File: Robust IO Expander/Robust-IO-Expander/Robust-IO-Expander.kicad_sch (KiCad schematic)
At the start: 54 parts, among them J1 Input Headers, J2 Chip Select Input, J3 Power Input, J4 SPI Input, J5 Screw_Terminal_01x16, J6 Output Screw Terminal, J7 Ouput Headers, J8 Power Input, U1 MCP23S17_SS, U10 LTV-847S, U2 MCP23S17_SS, U3 LTV-847S, U4 LTV-847S, U5 LTV-847S, U6 LTV-847S, U7 LTV-847S, U8 LTV-847S, U9 LTV-847S

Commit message: update
AD 09/10/23

finished schematic and all components on board
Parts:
- removed J3: Power Input, Connector_PinSocket_2.54mm:PinSocket_1x02_P2.54mm_Vertical, symbol Connector:Conn_01x02_Pin
- removed J8: Power Input, symbol Connector:Screw_Terminal_01x02
- added C1: 10uF, Capacitor_SMD:C_1206_3216Metric_Pad1.33x1.80mm_HandSolder, symbol Device:C_Polarized_Small
- added C2: 22uF, Capacitor_SMD:C_1206_3216Metric_Pad1.33x1.80mm_HandSolder, symbol Device:C_Polarized_Small
- added J10: Right SPI In, Connector_PinSocket_2.54mm:PinSocket_1x04_P2.54mm_Horizontal, symbol Connector:Conn_01x04_Socket
- added J11: SPI Inputs, TerminalBlock_Phoenix:TerminalBlock_Phoenix_MKDS-1,5-3_1x03_P5.00mm_Horizontal, symbol Connector:Screw_Terminal_01x03
- added J12: Power Input, Connector_PinSocket_2.54mm:PinSocket_1x03_P2.54mm_Vertical, symbol Connector:Conn_01x03_Pin
- added J3: CS Inputs, TerminalBlock_Phoenix:TerminalBlock_Phoenix_MKDS-1,5-2_1x02_P5.00mm_Horizontal, symbol Connector:Screw_Terminal_01x02
- added J8: Power Input, TerminalBlock_Phoenix:TerminalBlock_Phoenix_MKDS-1,5-3-5.08_1x03_P5.08mm_Horizontal, symbol Connector:Screw_Terminal_01x03
- added J9: Left SPI Out, Connector_PinHeader_2.54mm:PinHeader_1x04_P2.54mm_Horizontal, symbol Connector:Conn_01x04_Pin
- added U11: AMS1117-3.3, Package_TO_SOT_SMD:SOT-223-3_TabPin2, symbol Regulator_Linear:AMS1117-3.3
- J2: value Chip Select Input -> CS Inputs
- J4: value SPI Input -> SPI Inputs; footprint (none) -> Connector_PinSocket_2.54mm:PinSocket_1x03_P2.54mm_Vertical
- J5: value Screw_Terminal_01x16 -> Input Screw Terminal; footprint (none) -> TerminalBlock_Phoenix:TerminalBlock_Phoenix_MKDS-1,5-16_1x16_P5.00mm_Horizontal
- J6: footprint (none) -> TerminalBlock_Phoenix:TerminalBlock_Phoenix_MKDS-1,5-16_1x16_P5.00mm_Horizontal
- J7: footprint (none) -> Connector_PinSocket_2.54mm:PinSocket_1x16_P2.54mm_Vertical
- R1, R10, R11, R12, R13, R14, R15, R16, R17, R18, R19, R2, R20, R21, R22, R23, R24, R25, R26, R27, R28, R29, R3, R30, R31, R32, R4, R5, R6, R7, R8, R9: footprint (none) -> Resistor_SMD:R_0603_1608Metric_Pad0.98x0.95mm_HandSolder
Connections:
- net GND: now also C1.2, C2.2, J10.4 (Pin_4), J12.3 (Pin_3), J8.3 (Pin_3), J9.4 (Pin_4), U11.1 (GND)
- net InCS: now also J3.1 (Pin_1)
- net MISO: now also J10.3 (Pin_3), J11.3 (Pin_3), J9.3 (Pin_3)
- net MOSI: now also J10.2 (Pin_2), J11.2 (Pin_2), J9.2 (Pin_2)
- net OutCS: now also J3.2 (Pin_2)
- net SCK: now also J10.1 (Pin_1), J11.1 (Pin_1), J9.1 (Pin_1)
- net VCC: now also C1.1, J12.1 (Pin_1), J8.1 (Pin_1), U11.3 (VI); no longer U1.9 (VDD), U10.10, U10.12, U10.14, U10.16, U2.9 (VDD), U3.10, U3.12, U3.14, U3.16, U4.10, U4.12, U4.14, U4.16, U5.10, U5.12, U5.14, U5.16, U6.10, U6.12, U6.14, U6.16, U7.10, U7.12, U7.14, U7.16, U8.10, U8.12, U8.14, U8.16, U9.10, U9.12, U9.14, U9.16
- new net +24V: J12.2 (Pin_2), J8.2 (Pin_2), U10.10, U10.12, U10.14, U10.16, U7.10, U7.12, U7.14, U7.16, U8.10, U8.12, U8.14, U8.16, U9.10, U9.12, U9.14, U9.16
- new net +3.3V: C2.1, U1.9 (VDD), U11.2 (VO), U2.9 (VDD), U3.10, U3.12, U3.14, U3.16, U4.10, U4.12, U4.14, U4.16, U5.10, U5.12, U5.14, U5.16, U6.10, U6.12, U6.14, U6.16
- no-connect marks 0 -> 12
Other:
- note added: "10uF Tantalum Capacitor T491A106K020AT"
- note added: "22uF Tantalum Capacitor TAJA226M016RNJ"
- note added: "AMS1117 3.3V Voltage Regulator"
- note added: "I/O CONNECTORS"
- note added: "Power"
- note added: "SPI Connectors"
- note removed: "CONNECTORS"
- moved on the sheet: H1, H2, H3, J1, J2, J4, J5, J6, J7, R1, R10, R11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

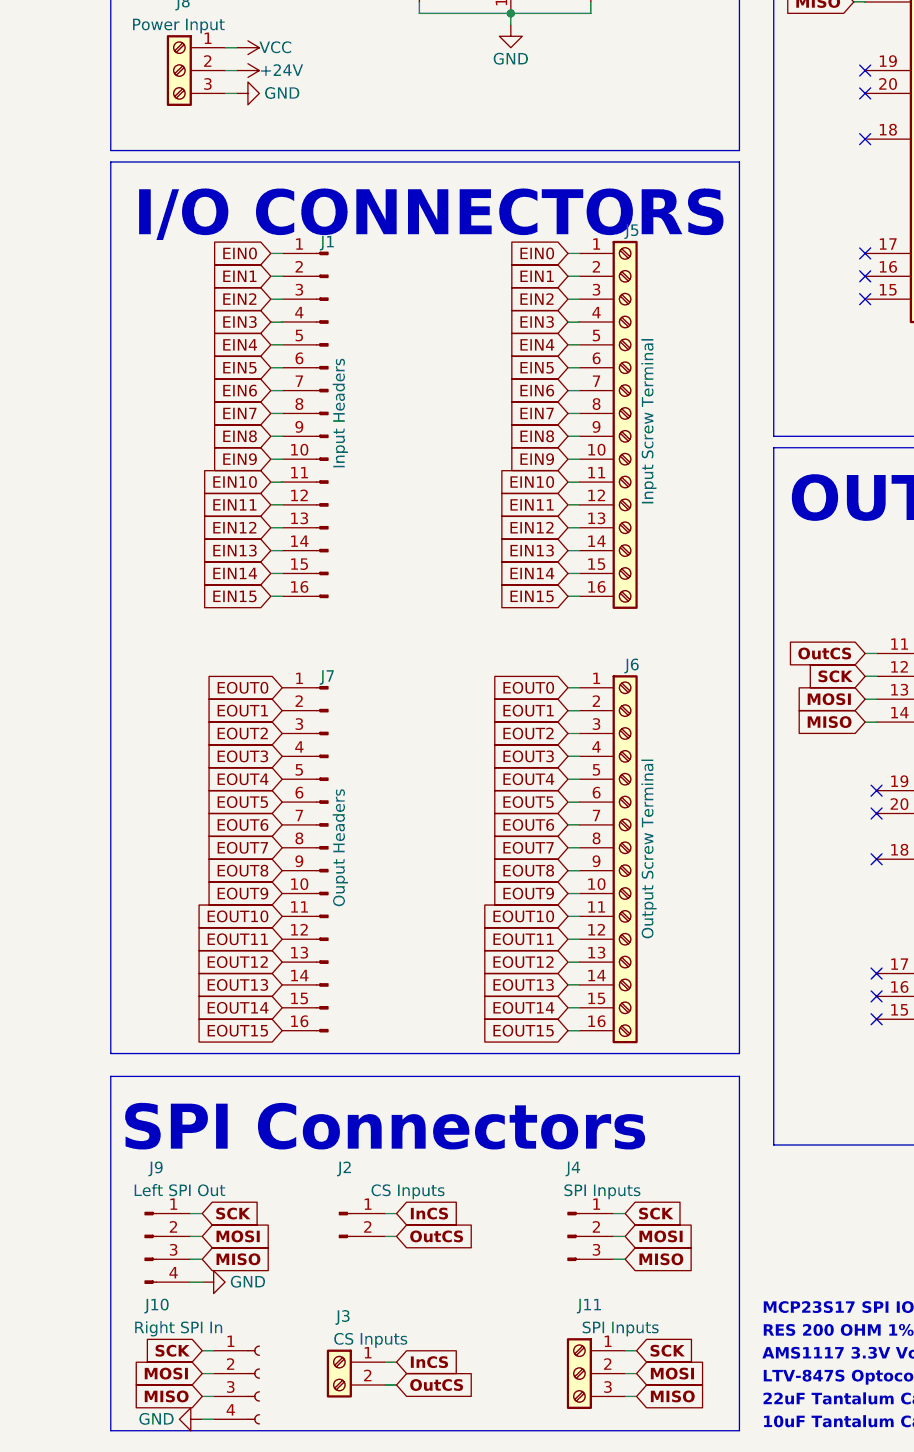
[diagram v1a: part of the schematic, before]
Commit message: Layout change
AD 15/10/23: Add Screw terminals everywhere
ESD Protection on IO and SPI Inputs
3.3v Regulator for IO power
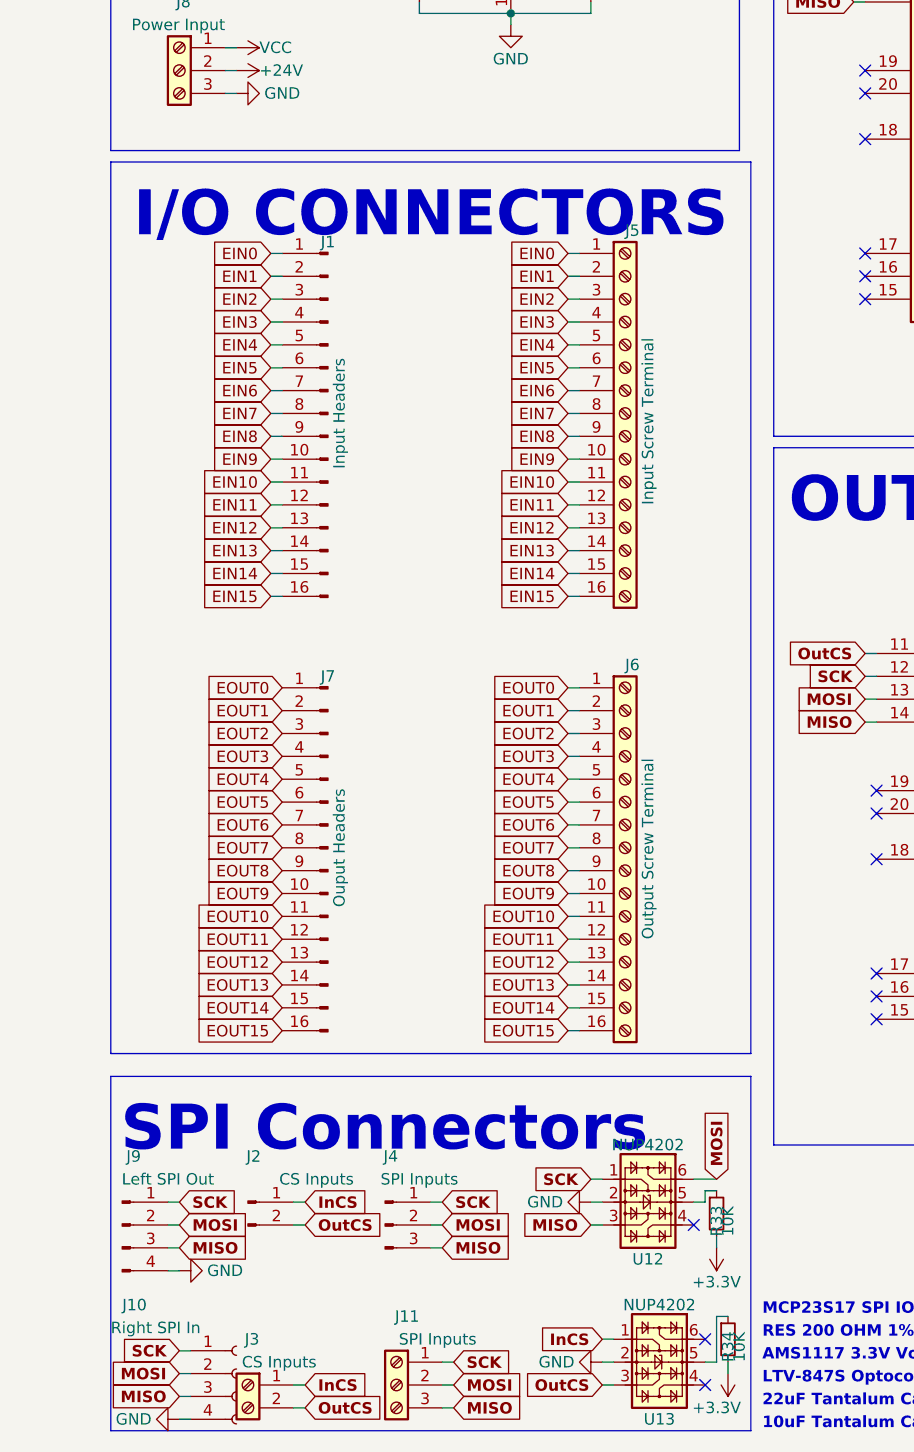
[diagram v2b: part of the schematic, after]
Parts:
- added R33, R34: 10K, Resistor_SMD:R_0603_1608Metric_Pad0.98x0.95mm_HandSolder, symbol Device:R_Small
- added U12, U13: NUP4202, Package_TO_SOT_SMD:SOT-363_SC-70-6, symbol Power_Protection:NUP4202
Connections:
- net +3.3V: now also R33.2, R34.2
- net GND: now also U12.2, U13.2
- net InCS: now also U13.1
- net MISO: now also U12.3
- net MOSI: now also U12.6
- net OutCS: now also U13.3
- net SCK: now also U12.1
- new net: R34.1, U13.5
- new net: R33.1, U12.5
- no-connect marks 12 -> 15
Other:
- moved on the sheet: J10, J11, J2, J3, J4, J9

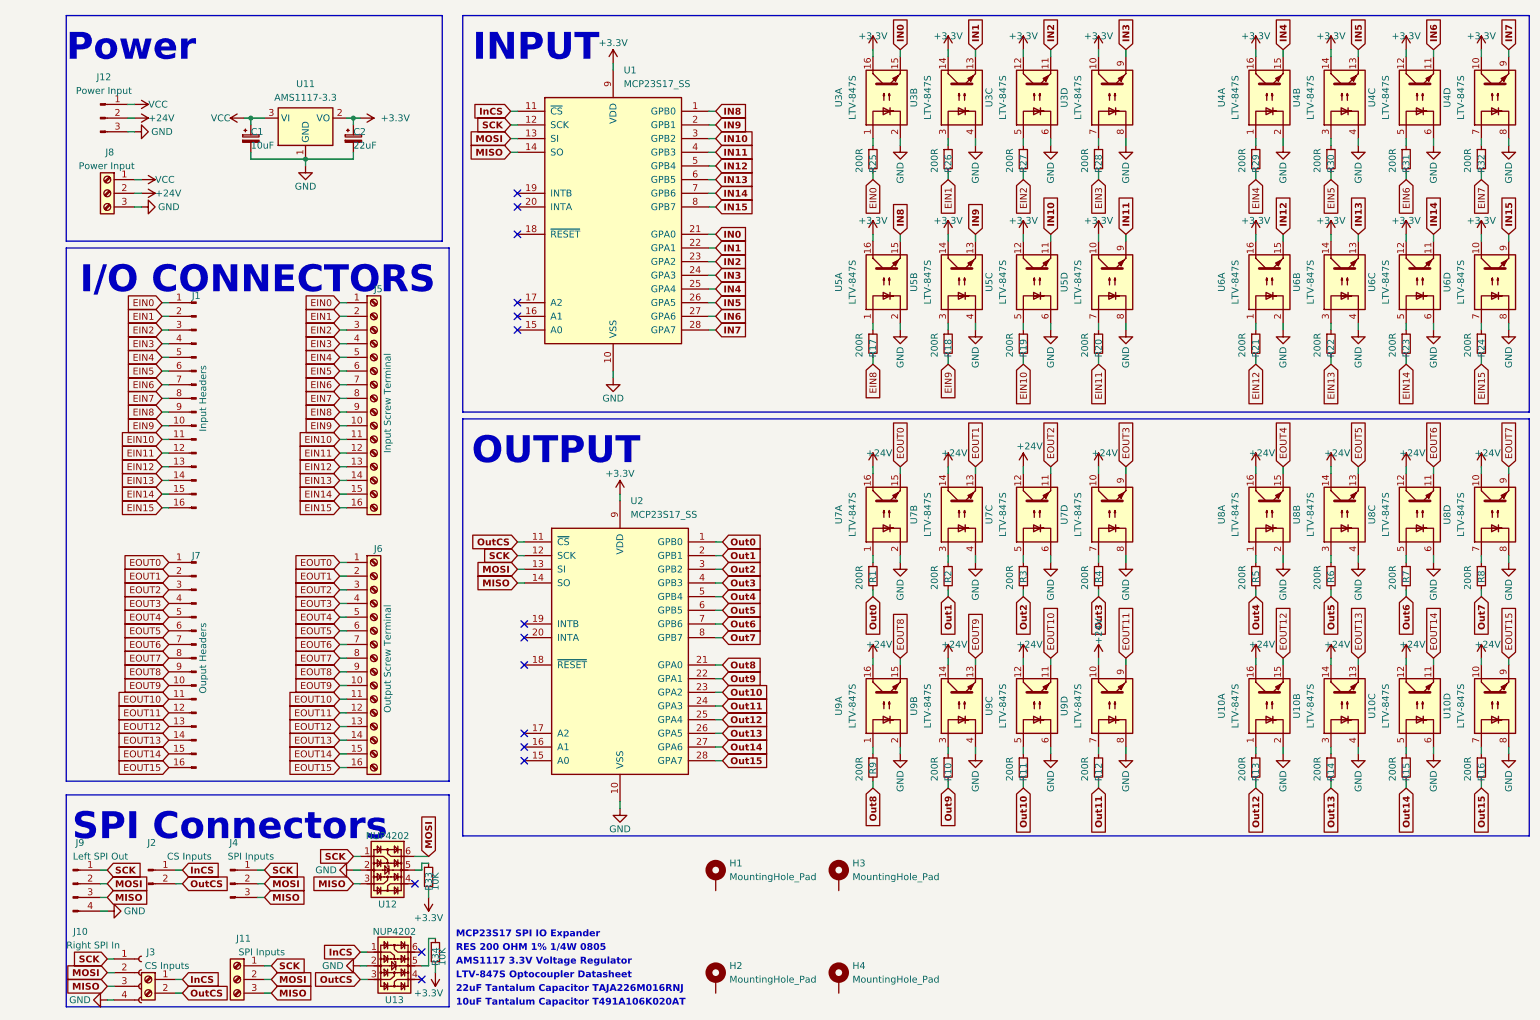
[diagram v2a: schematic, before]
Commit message: Design Complete
AD 10/12/23:
Design Finalised
BOM Created
Gerber and POS Files Generate
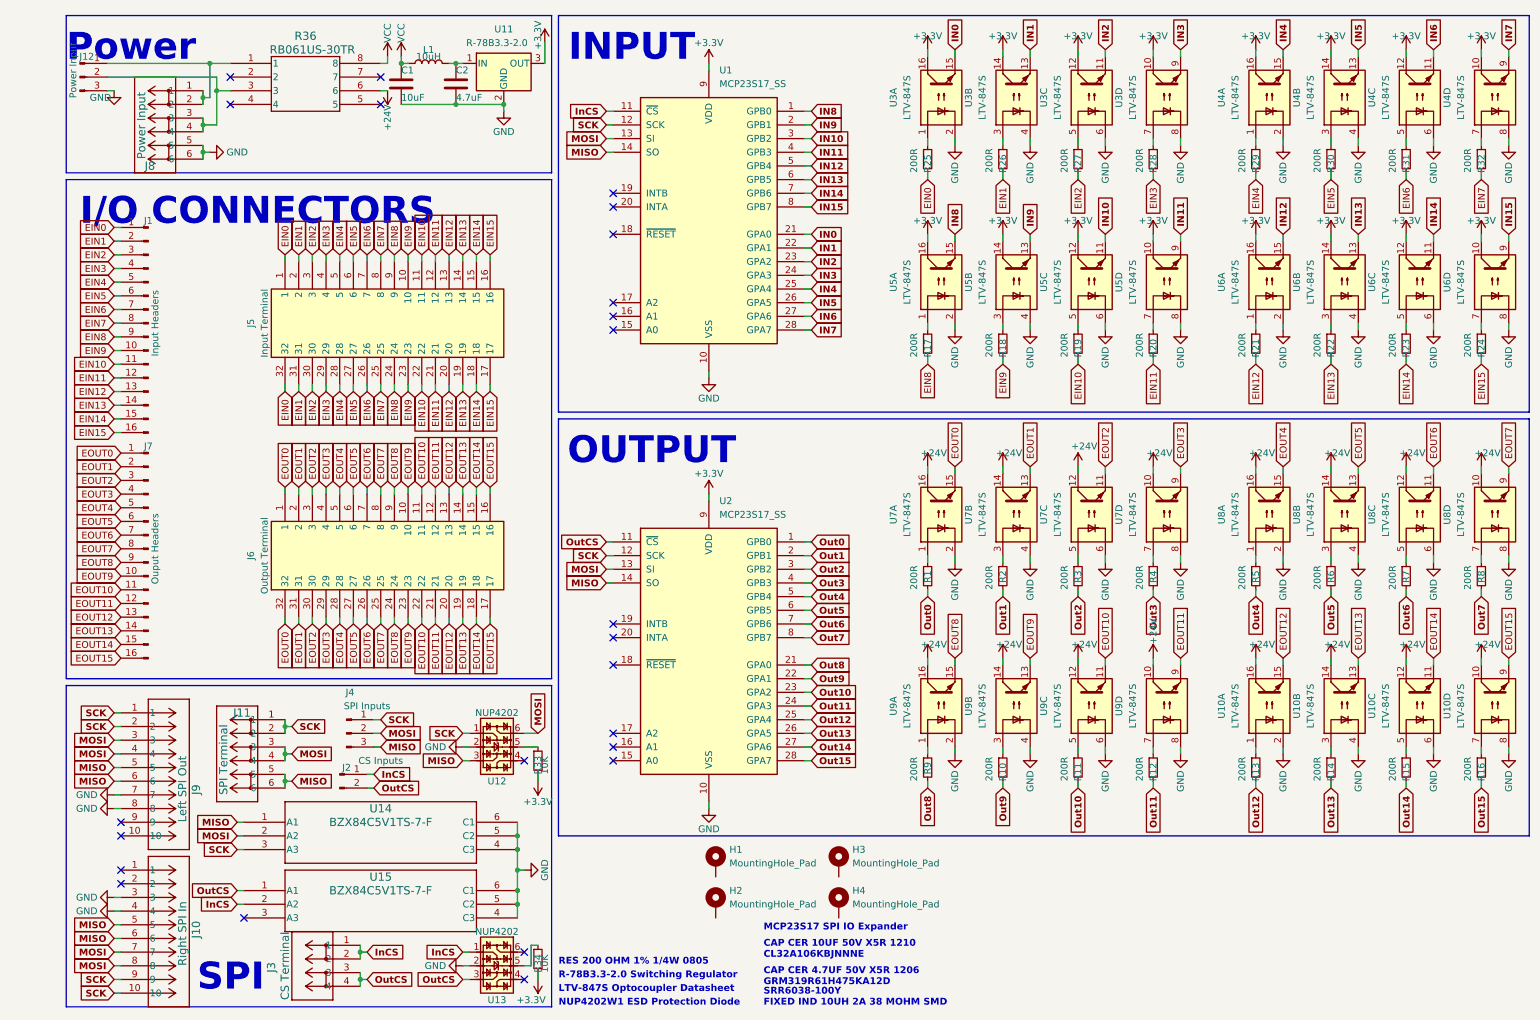
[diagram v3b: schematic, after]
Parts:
- removed C1: 10uF, Capacitor_SMD:C_1206_3216Metric_Pad1.33x1.80mm_HandSolder, symbol Device:C_Polarized_Small
- removed C2: 22uF, Capacitor_SMD:C_1206_3216Metric_Pad1.33x1.80mm_HandSolder, symbol Device:C_Polarized_Small
- removed J10: Right SPI In, Connector_PinSocket_2.54mm:PinSocket_1x04_P2.54mm_Horizontal, symbol Connector:Conn_01x04_Socket
- removed J11: SPI Inputs, TerminalBlock_Phoenix:TerminalBlock_Phoenix_MKDS-1,5-3_1x03_P5.00mm_Horizontal, symbol Connector:Screw_Terminal_01x03
- removed J3: CS Inputs, TerminalBlock_Phoenix:TerminalBlock_Phoenix_MKDS-1,5-2_1x02_P5.00mm_Horizontal, symbol Connector:Screw_Terminal_01x02
- removed J5: Input Screw Terminal, TerminalBlock_Phoenix:TerminalBlock_Phoenix_MKDS-1,5-16_1x16_P5.00mm_Horizontal, symbol Connector:Screw_Terminal_01x16
- removed J6: Output Screw Terminal, TerminalBlock_Phoenix:TerminalBlock_Phoenix_MKDS-1,5-16_1x16_P5.00mm_Horizontal, symbol Connector:Screw_Terminal_01x16
- removed J8: Power Input, TerminalBlock_Phoenix:TerminalBlock_Phoenix_MKDS-1,5-3-5.08_1x03_P5.08mm_Horizontal, symbol Connector:Screw_Terminal_01x03
- removed J9: Left SPI Out, Connector_PinHeader_2.54mm:PinHeader_1x04_P2.54mm_Horizontal, symbol Connector:Conn_01x04_Pin
- removed U11: AMS1117-3.3, Package_TO_SOT_SMD:SOT-223-3_TabPin2, symbol Regulator_Linear:AMS1117-3.3
- added C1: 10uF, Capacitor_SMD:C_1210_3225Metric_Pad1.33x2.70mm_HandSolder, symbol Device:C
- added C2: 4.7uF, Capacitor_SMD:C_1206_3216Metric_Pad1.33x1.80mm_HandSolder, symbol Device:C
- added J10: Right SPI In, LS2_105_01_F_D_RA2 footprint:CONN_LS2-105-01-X-D-RA2_SAI, symbol LS2_105_01_F_D_RA2:LS2-105-01-F-D-RA2
- added J11: SPI Terminal, 1862055 footprint:CONN_1862055, symbol 1862055:1862055
- added J3: CS Terminal, 1862042 footprint:CONN_1862042, symbol 1862042:1862042
- added J5: Input Terminal, 1862262 footprint:1862262, symbol 1862262:1862262
- added J6: Output Terminal, 1862262 footprint:1862262, symbol 1862262:1862262
- added J8: Power Input, 1862055 footprint:CONN_1862055, symbol 1862055:1862055
- added J9: Left SPI Out, LS2_105_01_F_D_RA1 footprint:CONN_LS2-105-01-X-D-RA1_SAI, symbol LS2_105_01_F_D_RA1:LS2-105-01-F-D-RA1
- added L1: 10uH, SRR6038_100Y footprint:IND_BOURNS_SRR6038, symbol Device:L
- added R36: RB061US-30TR, RB061US_30TR footprints:DIO_RB061U_ROM, symbol RB061US_30TR:RB061US-30TR
- added U11: R-78B3.3-2.0, Converter_DCDC:Converter_DCDC_RECOM_R-78B-2.0_THT, symbol Regulator_Switching:R-78B3.3-2.0
- added U14, U15: BZX84C5V1TS-7-F, footprints:SOT-363_DIO, symbol 2023-10-15_10-10-35:BZX84C5V1TS-7-F
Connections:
- net +24V: now also R36.6; no longer J12.2 (Pin_2)
- net +3.3V: now also U11.3 (OUT)
- net EIN0: now also J5.1, J5.32
- net EIN1: now also J5.2, J5.31
- net EIN10: now also J5.11, J5.22
- net EIN11: now also J5.12, J5.21
- net EIN12: now also J5.13, J5.20
- net EIN13: now also J5.14, J5.19
- net EIN14: now also J5.15, J5.18
- net EIN15: now also J5.16, J5.17
- net EIN2: now also J5.3, J5.30
- net EIN3: now also J5.29, J5.4
- net EIN4: now also J5.28, J5.5
- net EIN5: now also J5.27, J5.6
- net EIN6: now also J5.26, J5.7
- net EIN7: now also J5.25, J5.8
- net EIN8: now also J5.24, J5.9
- net EIN9: now also J5.10, J5.23
- net EOUT0: now also J6.1, J6.32
- net EOUT1: now also J6.2, J6.31
- net EOUT10: now also J6.11, J6.22
- net EOUT11: now also J6.12, J6.21
- net EOUT12: now also J6.13, J6.20
- net EOUT13: now also J6.14, J6.19
- net EOUT14: now also J6.15, J6.18
- net EOUT15: now also J6.16, J6.17
- net EOUT2: now also J6.3, J6.30
- net EOUT3: now also J6.29, J6.4
- net EOUT4: now also J6.28, J6.5
- net EOUT5: now also J6.27, J6.6
- net EOUT6: now also J6.26, J6.7
- net EOUT7: now also J6.25, J6.8
- net EOUT8: now also J6.24, J6.9
- net EOUT9: now also J6.10, J6.23
- net GND: now also C1.2, C2.2, J10.3, J10.4, J8.5, J8.6, J9.7, J9.8, U11.2 (GND), U14.4 (C3), U14.5 (C2), U14.6 (C1), U15.4 (C3), U15.5 (C2), U15.6 (C1)
- net InCS: now also J3.1, J3.2, U15.2 (A2)
- net MISO: now also J10.5, J10.6, J11.5, J11.6, J9.5, J9.6, U14.1 (A1)
- net MOSI: now also J10.7, J10.8, J11.3, J11.4, J9.3, J9.4, U14.2 (A2)
- net OutCS: now also J3.3, J3.4, U15.1 (A1)
- net SCK: now also J10.10, J10.9, J11.1, J11.2, J9.1, J9.2, U14.3 (A3)
- net VCC: now also C1.1, L1.1, R36.8; no longer J12.1 (Pin_1)
- new net: C2.1, L1.2, U11.1 (IN)
- new net: J12.1 (Pin_1), J8.1, J8.2, R36.1
- new net: J12.2 (Pin_2), J8.3, J8.4, R36.3
- no-connect marks 15 -> 24
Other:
- note added: "CAP CER 10UF 50V X5R 1210 CL32A106KBJNNNE"
- note added: "CAP CER 4.7UF 50V X5R 1206 GRM319R61H475KA12D"
- note added: "NUP4202W1 ESD Protection Diode"
- note added: "R-78B3.3-2.0 Switching Regulator"
- note added: "SPI"
- note added: "SRR6038-100Y FIXED IND 10UH 2A 38 MOHM SMD"
- note removed: "10uF Tantalum Capacitor T491A106K020AT"
- note removed: "22uF Tantalum Capacitor TAJA226M016RNJ"
- note removed: "AMS1117 3.3V Voltage Regulator"
- note removed: "SPI Connectors"
- moved on the sheet: H1, H2, H3, H4, J1, J12, J2, J4, J7, R1, R10, R11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
